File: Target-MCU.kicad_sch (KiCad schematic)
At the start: 18 parts, among them Q6 DMG1012UW-7, SW5 SKRPASE010

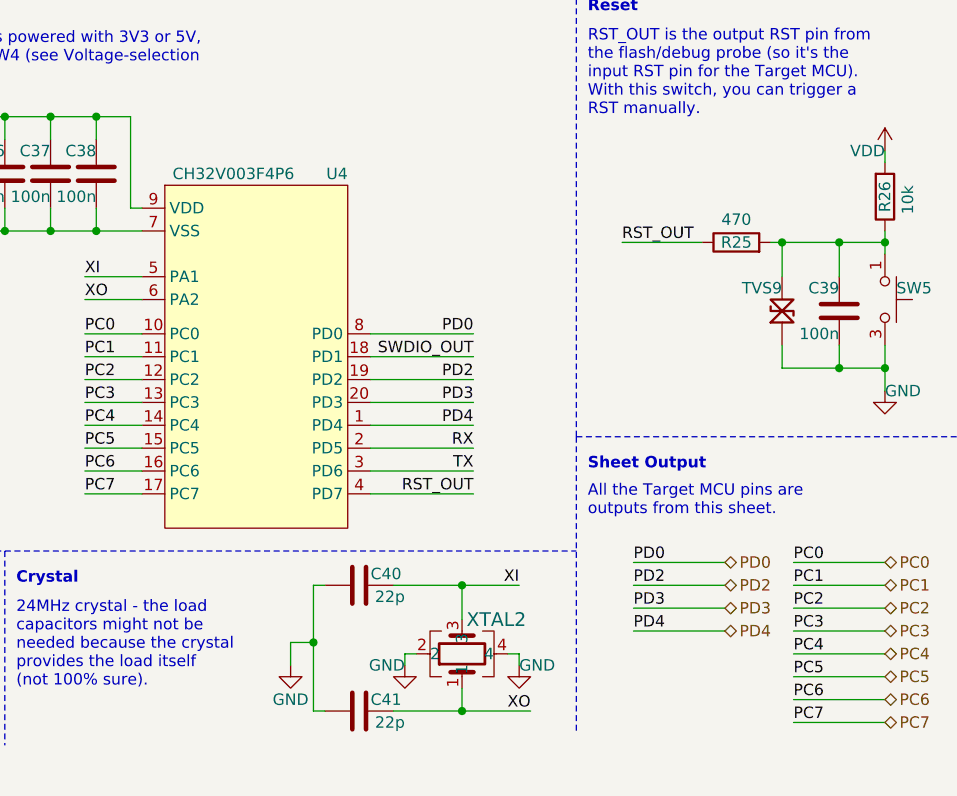
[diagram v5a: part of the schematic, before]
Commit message: Prefix each symbol name in library - eg. 'D_', 'CONN_', 'IC_', ...
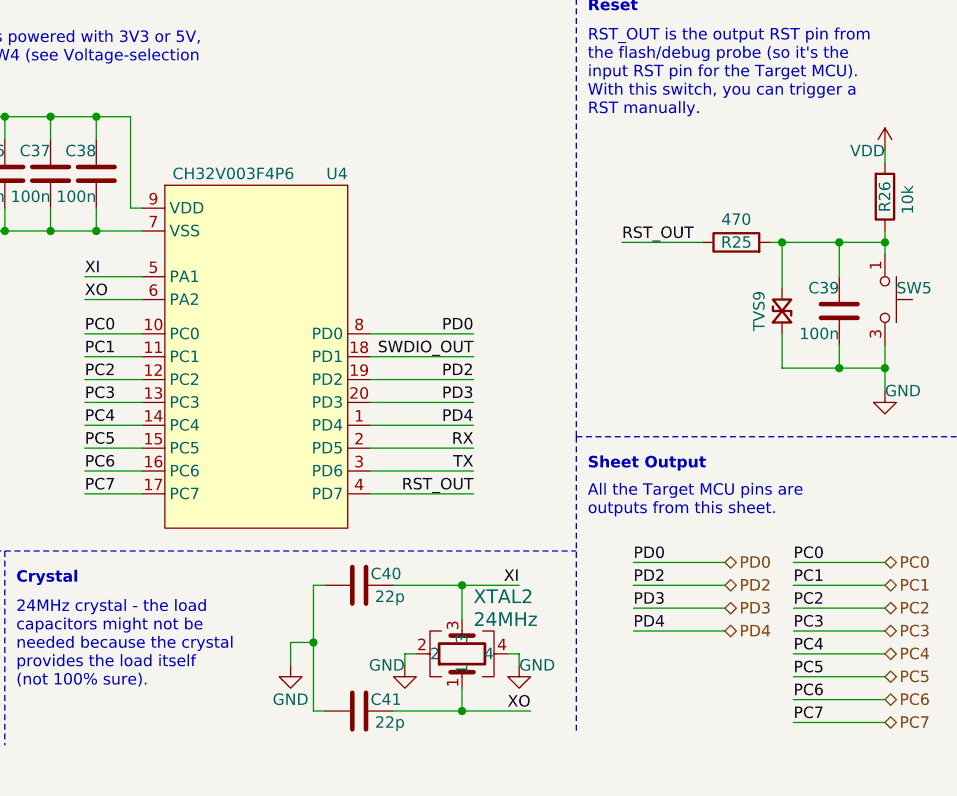
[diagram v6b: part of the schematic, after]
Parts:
- removed TVS9: 5V, Tiny_Scarab:D_SOD-323_CDSOD323-T05LC, symbol Tiny_Scarab:CDSOD323-T05LC
- added TVS9: 5V, Tiny_Scarab:D_SOD-882_SP1007-01ETG, symbol Tiny_Scarab:TVS_SP1007-01ETG
- SW5: value SKRPASE010 -> 16V 50mA; symbol Tiny_Scarab:SKRPASE010 -> Tiny_Scarab:SW_SKRPASE010; SPN 4809-SKRPADE010TR-ND -> (none); Supplier DigiKey -> (none)
- U4: value ~ -> CH32V003F4P6; symbol Tiny_Scarab:CH32V003F4P6 -> Tiny_Scarab:IC_CH32V003F4P6
- XTAL2: value M24000J054 -> 24MHz; symbol Tiny_Scarab:M24000J054 -> Tiny_Scarab:XTAL_M24000J054
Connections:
- net GND: now also TVS9.2
- net at C39.1, R25.2, R26.1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: now also TVS9.1
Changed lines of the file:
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@@
-    (stroke (width 0) (type default))
-  )
-  (wire (pts (xy 176.53 48.26) (xy 176.53 52.07))
     (stroke (width 0) (type default))
   )
@@
     (stroke (width 0) (type default))
   )
-  (wire (pts (xy 176.53 59.69) (xy 176.53 62.23))
+  (wire (pts (xy 176.53 58.42) (xy 176.53 62.23))
     (stroke (width 0) (type default))
   )
@@
   )
   (wire (pts (xy 82.55 34.29) (xy 82.55 33.02))
+    (stroke (width 0) (type default))
+  )
+  (wire (pts (xy 176.53 48.26) (xy 176.53 53.34))
     (stroke (width 0) (type default))
   )
@@
     (effects (font (size 1.27 1.27)) (justify right))
   )
-  (symbol (lib_id "Tiny_Scarab:CDSOD323-T05LC") (at 176.53 55.88 0) (unit 1)
-    (in_bom yes) (on_board yes) (dnp no)
-    (property "Reference" "TVS9" (at 176.53 53.34 0)
-      (effects (font (size 1.27 1.27)) (justify right))
-    )
-    (property "Value" "5V" (at 177.8 59.69 0)
-      (effects (font (size 0.5 0.5)) (justify left) hide)
-    )
-    (property "Footprint" "Tiny_Scarab:D_SOD-323_CDSOD323-T05LC" (at 186.69 49.53 0)
-      (effects (font (size 1.27 1.27)) (justify left bottom) hide)
-    )
-    (property "Datasheet" "https://www.bourns.com/docs/Product-Datasheets/CDSOD323-TxxLC.pdf" (at 186.69 52.07 0)
-      (effects (font (size 1.27 1.27)) (justify left) hide)
-    )
-    (property "Manufacturer" "Bourns" (at 186.69 55.88 0)
-      (effects (font (size 1.27 1.27)) (justify left bottom) hide)
-    )
-    (property "MPN" "CDSOD323-T05LC" (at 186.69 58.42 0)
-      (effects (font (size 1.27 1.27)) (justify left bottom) hide)
-    )
-    (property "JLCPCB Part #" "C840637" (at 176.53 55.88 0)
-      (effects (font (size 1.27 1.27)) hide)
-    )
-    (property "DigiKey" "CDSOD323-T05LCTR-ND" (at 165.1 43.18 0)
-      (effects (font (size 1.27 1.27)) (justify left) hide)
-    )
-    (property "Farnell" "1824861" (at 176.53 41.91 0)
-      (effects (font (size 1.27 1.27)) hide)
-    )
-    (property "Mouser" "652-CDSOD323-T05LC" (at 176.53 44.45 0)
-      (effects (font (size 1.27 1.27)) hide)
-    )
-    (pin "2")
-    (pin "1")
-    (instances
-      (project "tiny-scarab"
-        (path "/156c5422-ee07-49a4-8263-a2dbd26b90bd/d0c4b0c3-1e7e-4a4c-add3-8d4a3a10843d"
-          (reference "TVS9") (unit 1)
-        )
-      )
-    )
-  )
-  (symbol (lib_id "Tiny_Scarab:SKRPASE010") (at 187.96 54.61 270) (unit 1)
+  (symbol (lib_id "Tiny_Scarab:SW_SKRPASE010") (at 187.96 54.61 270) (unit 1)
     (in_bom yes) (on_board yes) (dnp no)
     (property "Reference" "SW5" (at 189.23 53.34 90)
       (effects (font (size 1.27 1.27)) (justify left))
     )
-    (property "Value" "SKRPASE010" (at 196.85 54.61 0)
-      (effects (font (size 1.27 1.27)) hide)
-    )
-    (property "Footprint" "Tiny_Scarab:SW_Tactile_SPST_NO_Straight_ALPSALPINE_SKRP" (at 214.63 53.34 0)
-      (effects (font (size 1.27 1.27)) hide)
-    )
-    (property "Datasheet" "https://www.farnell.com/datasheets/2864500.pdf" (at 212.09 54.61 0)
-      (effects (font (size 1.27 1.27)) hide)
-    )
-    (property "Manufacturer" "ALPSALPINE" (at 209.55 54.61 0)
-      (effects (font (size 1.27 1.27)) hide)
-    )
-    (property "MPN" "SKRPASE010" (at 207.01 54.61 0)
-      (effects (font (size 1.27 1.27)) hide)
-    )
-    (property "Supplier" "DigiKey" (at 204.47 54.61 0)
-      (effects (font (size 1.27 1.27)) hide)
-    )
-    (property "SPN" "4809-SKRPADE010TR-ND" (at 201.93 54.61 0)
-      (effects (font (size 1.27 1.27)) hide)
-    )
-    (property "JLCPCB Part #" "C470427" (at 199.39 54.61 0)
+    (property "Value" "16V 50mA" (at 213.36 54.61 0)
+      (effects (font (size 1.27 1.27)) hide)
+    )
+    (property "Footprint" "Tiny_Scarab:SW_Tactile_SPST_NO_Straight_ALPSALPINE_SKRP" (at 215.9 54.61 0)
+      (effects (font (size 1.27 1.27)) hide)
+    )
+    (property "Datasheet" "https://www.farnell.com/datasheets/2864500.pdf" (at 210.82 54.61 0)
+      (effects (font (size 1.27 1.27)) hide)
+    )
+    (property "Manufacturer" "ALPSALPINE" (at 208.28 54.61 0)
+      (effects (font (size 1.27 1.27)) hide)
+    )
+    (property "MPN" "SKRPASE010" (at 205.74 54.61 0)
+      (effects (font (size 1.27 1.27)) hide)
+    )
+    (property "JLCPCB Part #" "C470427" (at 203.2 54.61 0)
       (effects (font (size 1.27 1.27)) hide)
     )
@@
     )
   )
-  (symbol (lib_id "Tiny_Scarab:CH32V003F4P6") (at 118.11 57.15 0) (unit 1)
+  (symbol (lib_id "Tiny_Scarab:IC_CH32V003F4P6") (at 118.11 57.15 0) (unit 1)
     (in_bom yes) (on_board yes) (dnp no)
     (property "Reference" "U4" (at 128.27 40.64 0)
       (effects (font (size 1.27 1.27)) (justify right))
     )
-    (property "Value" "~" (at 115.57 40.64 0)
-      (effects (font (size 1.27 1.27)) hide)
+    (property "Value" "CH32V003F4P6" (at 115.57 40.64 0)
+      (effects (font (size 1.27 1.27)))
     )
     (property "Footprint" "Package_SO:TSSOP-20_4.4x6.5mm_P0.65mm" (at 119.38 82.55 0)
@@
       (effects (font (size 1.27 1.27)) hide)
     )
-    (property "Manufacturer" "WCH" (at 118.11 57.15 0)
-      (effects (font (size 1.27 1.27)) hide)
-    )
-    (property "MPN" "CH32V003F4P6" (at 115.57 40.64 0)
-      (effects (font (size 1.27 1.27)))
+    (property "Manufacturer" "WCH" (at 118.11 25.4 0)
+      (effects (font (size 1.27 1.27)) hide)
+    )
+    (property "MPN" "CH32V003F4P6" (at 118.11 27.94 0)
+      (effects (font (size 1.27 1.27)) hide)
     )
     (property "Supplier" "AliExpress" (at 118.11 57.15 0)
@@
       (effects (font (size 1.27 1.27)) hide)
     )
-    (property "JLCPCB Part #" "C5187096" (at 118.11 57.15 0)
+    (property "JLCPCB Part #" "C5187096" (at 118.11 30.48 0)
       (effects (font (size 1.27 1.27)) hide)
     )
@@
     )
     (property "DigiKey" "" (at 118.11 57.15 0)
-      (effects (font (size 1.27 1.27)))
+      (effects (font (size 1.27 1.27)) hide)
     )
     (property "Farnell" "" (at 118.11 57.15 0)
-      (effects (font (size 1.27 1.27)))
+      (effects (font (size 1.27 1.27)) hide)
     )
     (property "Mouser" "" (at 118.11 57.15 0)
-      (effects (font (size 1.27 1.27)))
+      (effects (font (size 1.27 1.27)) hide)
     )
     (pin "17")
@@
     )
   )
+  (symbol (lib_id "Tiny_Scarab:TVS_SP1007-01ETG") (at 176.53 55.88 0) (unit 1)
+    (in_bom yes) (on_board yes) (dnp no)
+    (property "Reference" "TVS9" (at 173.99 55.88 90)
+      (effects (font (size 1.27 1.27)))
+    )
+    (property "Value" "5V" (at 175.26 57.15 0)
+      (effects (font (size 1.27 1.27)) (justify right) hide)
+    )
+    (property "Footprint" "Tiny_Scarab:D_SOD-882_SP1007-01ETG" (at 176.53 33.02 0)
+      (effects (font (size 1.27 1.27)) (justify bottom) hide)
+    )
+    (property "Datasheet" "" (at 165.1 41.91 0)
+      (effects (font (size 1.27 1.27)) (justify left) hide)
+    )
+    (property "Manufacturer" "Littelfuse" (at 176.53 35.56 0)
+      (effects (font (size 1.27 1.27)) (justify bottom) hide)
+    )
+    (property "MPN" "SP1007-01ETG" (at 176.53 38.1 0)
+      (effects (font (size 1.27 1.27)) (justify bottom) hide)
+    )
+    (property "JLCPCB Part #" "C126836" (at 176.53 39.37 0)
+      (effects (font (size 1.27 1.27)) hide)
+    )
+    (property "DigiKey" "F6187TR-ND" (at 176.53 41.91 0)
+      (effects (font (size 1.27 1.27)) hide)
+    )
+    (property "Farnell" "2777317" (at 176.53 44.45 0)
+      (effects (font (size 1.27 1.27)) hide)
+    )
+    (property "Mouser" "576-SP1007-01ETG" (at 176.53 46.99 0)
+      (effects (font (size 1.27 1.27)) hide)
+    )
+    (pin "1")
+    (pin "2")
+    (instances
+      (project "tiny-scarab"
+        (path "/156c5422-ee07-49a4-8263-a2dbd26b90bd/d0c4b0c3-1e7e-4a4c-add3-8d4a3a10843d"
+          (reference "TVS9") (unit 1)
+        )
+      )
+    )
+  )
   (symbol (lib_id "Device:C") (at 129.54 100.33 90) (unit 1)
     (in_bom yes) (on_board yes) (dnp no)
@@
     )
   )
-  (symbol (lib_id "Tiny_Scarab:M24000J054") (at 140.97 93.98 90) (unit 1)
-    (in_bom yes) (on_board yes) (dnp no)
-    (property "Reference" "XTAL2" (at 144.78 90.17 90)
-      (effects (font (size 1.524 1.524)))
-    )
-    (property "Value" "M24000J054" (at 153.67 94.3041 90)
-      (effects (font (size 1.524 1.524)) hide)
+  (symbol (lib_id "Tiny_Scarab:XTAL_M24000J054") (at 140.97 93.98 90) (unit 1)
+    (in_bom yes) (on_board yes) (dnp no)
+    (property "Reference" "XTAL2" (at 142.24 87.63 90)
+      (effects (font (size 1.524 1.524)) (justify right))
+    )
+    (property "Value" "24MHz" (at 142.24 90.17 90)
+      (effects (font (size 1.524 1.524)) (justify right))
     )
     (property "Footprint" "Tiny_Scarab:CRYSTAL-SMD3225-4P" (at 109.22 93.98 0)
@@
       (effects (font (size 1.27 1.27) italic) hide)
     )
-    (property "Manufacturer" "ECEC(ZheJiang E ast Crystal Elec)" (at 114.3 93.98 0)
-      (effects (font (size 1.27 1.27)) hide)
-    )
-    (property "MPN" "M24000J054" (at 116.84 93.98 0)
-      (effects (font (size 1.27 1.27)) hide)
-    )
-    (property "JLCPCB Part #" "C279615" (at 128.27 93.98 0)
-      (effects (font (size 1.27 1.27)) hide)
-    )
+    (property "Manufacturer" "ECEC(ZheJiang E ast Crystal Elec)" (at 111.76 93.98 0)
+      (effects (font (size 1.27 1.27)) hide)
+    )
+    (property "MPN" "M24000J054" (at 114.3 93.98 0)
+      (effects (font (size 1.27 1.27)) hide)
+    )
+    (property "JLCPCB Part #" "C279615" (at 116.84 93.98 0)
+      (effects (font (size 1.27 1.27)) hide)
+    )

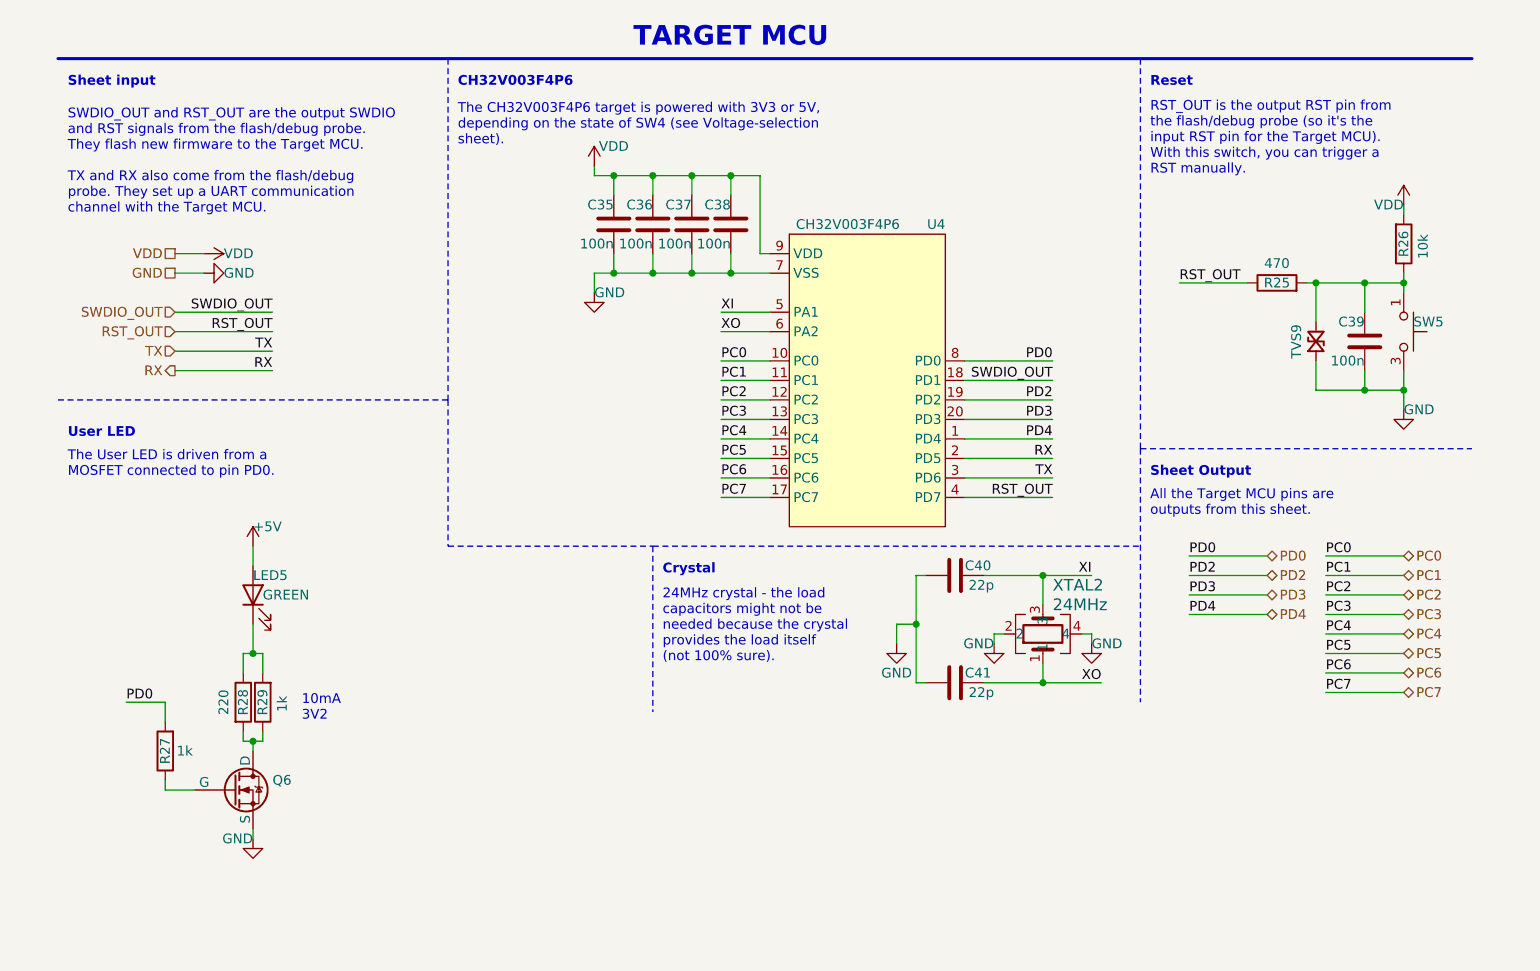
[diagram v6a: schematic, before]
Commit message: Rename net 'RST_OUT' into 'RST_CH32V003'
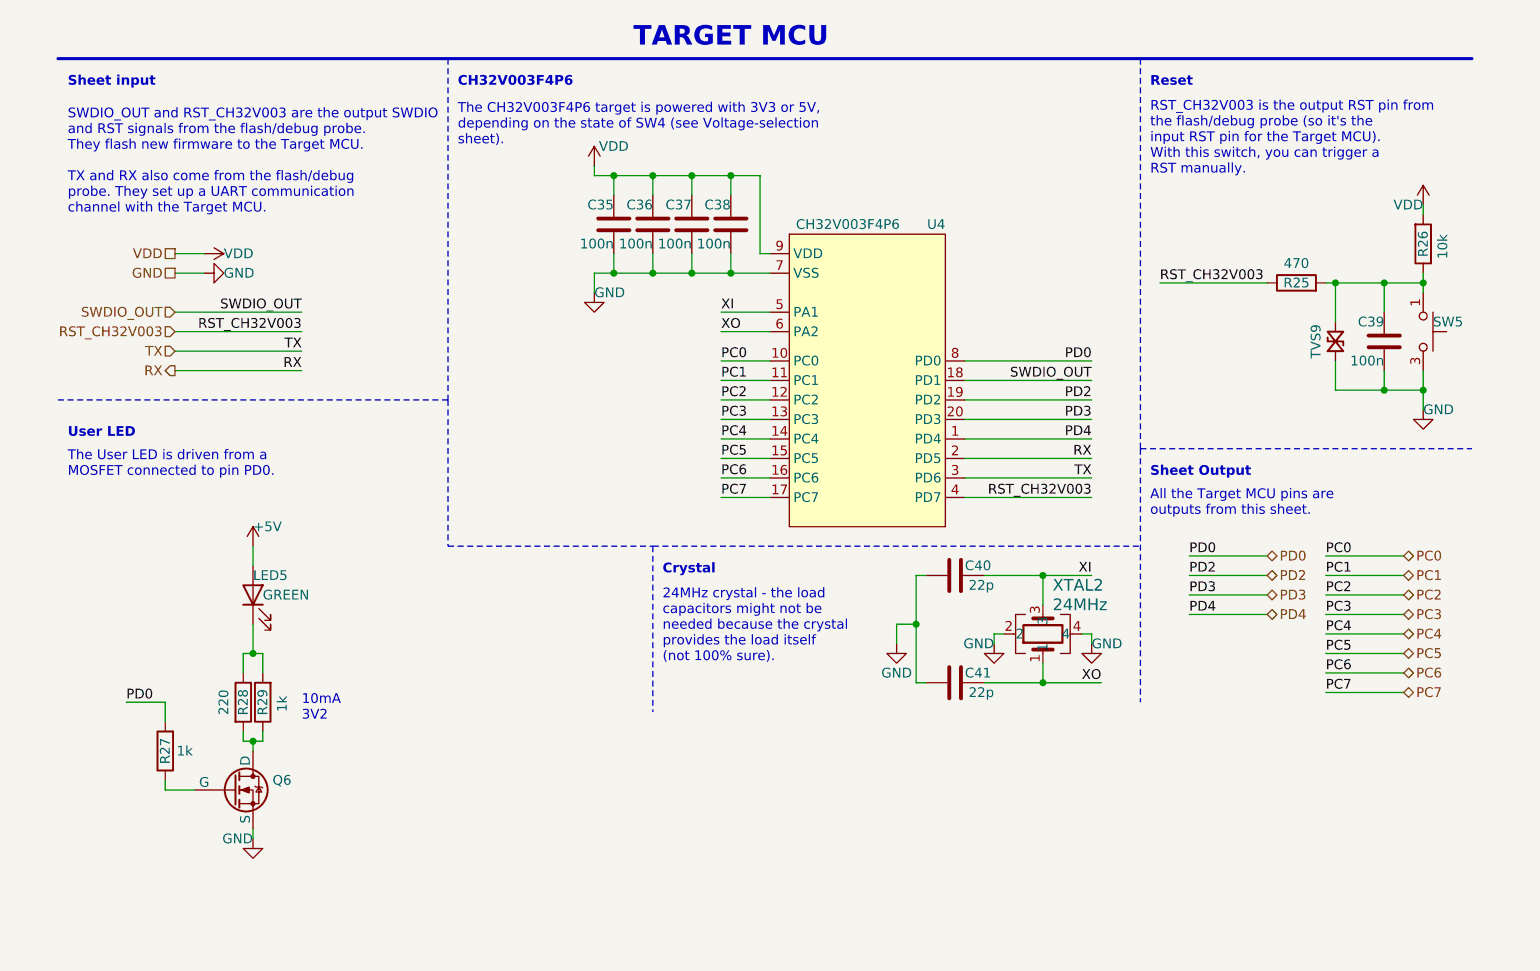
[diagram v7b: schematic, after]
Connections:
- net RST_OUT renamed RST_CH32V003
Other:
- note added: "RST_CH32V003 is the output RST pin from the flash/debug probe (so it's the input RST pin for the Target MCU). With this switch, you can trigger a RST manually."
- note added: "SWDIO_OUT and RST_CH32V003 are the output SWDIO and RST signals from the flash/debug probe. They flash new firmware to the Target MCU. TX and RX also come from the flash/debug probe. They set up a UART communication channel with the Target MCU."
- note removed: "RST_OUT is the output RST pin from the flash/debug probe (so it's the input RST pin for the Target MCU). With this switch, you can trigger a RST manually."
- note removed: "SWDIO_OUT and RST_OUT are the output SWDIO and RST signals from the flash/debug probe. They flash new firmware to the Target MCU. TX and RX also come from the flash/debug probe. They set up a UART communication channel with the Target MCU."
- moved on the sheet: C39, R25, R26, SW5, TVS9
